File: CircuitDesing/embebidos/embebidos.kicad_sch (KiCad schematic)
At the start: 0 parts

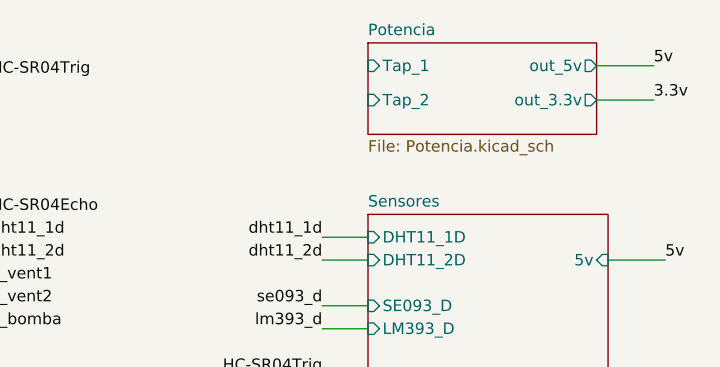
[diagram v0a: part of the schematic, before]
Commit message: pull up
Circuito LDR
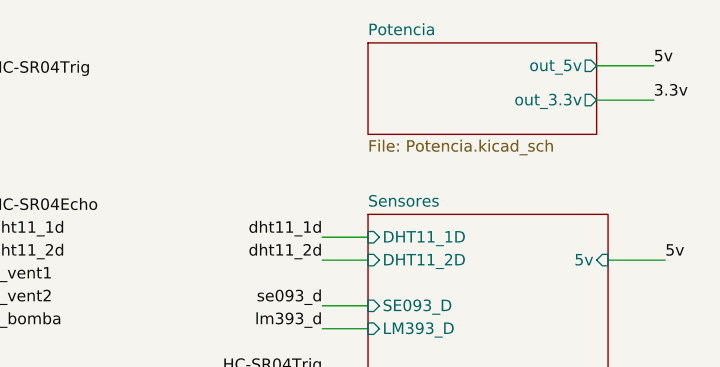
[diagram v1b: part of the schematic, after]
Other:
- sheet Potencia ports: added none; removed Tap_1, Tap_2
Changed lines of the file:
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@@
       (effects (font (size 1.27 1.27)) (justify left top))
-    )
-    (pin "Tap_1" input (at 167.64 62.23 180)
-      (effects (font (size 1.27 1.27)) (justify left))
-    )
-    (pin "Tap_2" input (at 167.64 66.04 180)
-      (effects (font (size 1.27 1.27)) (justify left))
     )
     (pin "out_5v" output (at 193.04 62.23 0)
@@
     (path "/baefe8d2-116f-4132-b22d-e866645ad738" (page "4"))
     (path "/2a66dc13-5d83-46f7-9074-3655609524a8" (page "5"))
-    (path "/2a66dc13-5d83-46f7-9074-3655609524a8/a135e9bb-3dd4-4bac-8875-0b8619cdbde0" (page "7"))
     (path "/2a66dc13-5d83-46f7-9074-3655609524a8/74549759-895a-4805-b4eb-8b7b7d22db26" (page "7"))
     (path "/4a4a8db1-1786-4804-b37e-204adf7255cc/49f3433d-4d41-4994-b007-3fd9fa4c7900" (page "8"))
@@
       (reference "#PWR015") (unit 1) (value "GND") (footprint "")
     )
-    (path "/2a66dc13-5d83-46f7-9074-3655609524a8/88b4c1f2-fa29-42b0-8b8e-d7a406d13c1c"
-      (reference "#PWR016") (unit 1) (value "GND") (footprint "")
-    )
-    (path "/2a66dc13-5d83-46f7-9074-3655609524a8/a135e9bb-3dd4-4bac-8875-0b8619cdbde0/f95e0a6a-1f02-4b13-a777-d73ecda7f4e6"
-      (reference "#PWR017") (unit 1) (value "GND") (footprint "")
-    )
-    (path "/2a66dc13-5d83-46f7-9074-3655609524a8/a135e9bb-3dd4-4bac-8875-0b8619cdbde0/093773d2-48d3-4183-9a42-2d4675e4bd31"
-      (reference "#PWR018") (unit 1) (value "GND") (footprint "")
-    )
-    (path "/2a66dc13-5d83-46f7-9074-3655609524a8/a135e9bb-3dd4-4bac-8875-0b8619cdbde0/cdabb997-2f53-4fa4-a27a-fd81b4d9f5ba"
-      (reference "#PWR019") (unit 1) (value "GND") (footprint "")
-    )
-    (path "/2a66dc13-5d83-46f7-9074-3655609524a8/a135e9bb-3dd4-4bac-8875-0b8619cdbde0/3d119db0-fa20-4eb6-83c6-89997012cb89"
-      (reference "#PWR020") (unit 1) (value "GND") (footprint "")
-    )
     (path "/2a66dc13-5d83-46f7-9074-3655609524a8/74549759-895a-4805-b4eb-8b7b7d22db26/e0179e21-6428-45da-b033-c9fefee37896"
       (reference "#PWR021") (unit 1) (value "GND") (footprint "")
@@
       (reference "#PWR0105") (unit 1) (value "GND") (footprint "")
     )
+    (path "/4a4a8db1-1786-4804-b37e-204adf7255cc/49f3433d-4d41-4994-b007-3fd9fa4c7900/07f61c9e-cf2f-4ff8-971f-bebff896dc30"
+      (reference "#PWR?") (unit 1) (value "GND") (footprint "")
+    )
+    (path "/2a66dc13-5d83-46f7-9074-3655609524a8/14cf2f17-a01d-473c-884e-3c66510750af"
+      (reference "#PWR?") (unit 1) (value "GND") (footprint "")
+    )
     (path "/4a4a8db1-1786-4804-b37e-204adf7255cc/49f3433d-4d41-4994-b007-3fd9fa4c7900/ba8244e2-67ae-47d6-acea-927aaf267f1a"
       (reference "7k1") (unit 1) (value "R") (footprint "Resistor_SMD:R_0603_1608Metric_Pad0.98x0.95mm_HandSolder")
@@
       (reference "10k2") (unit 1) (value "R") (footprint "Resistor_SMD:R_0603_1608Metric_Pad0.98x0.95mm_HandSolder")
     )
+    (path "/4a4a8db1-1786-4804-b37e-204adf7255cc/49f3433d-4d41-4994-b007-3fd9fa4c7900/a970a7de-87f7-4442-a266-d08deb9a3533"
+      (reference "10k?") (unit 1) (value "R") (footprint "Resistor_SMD:R_0603_1608Metric_Pad0.98x0.95mm_HandSolder")
+    )
+    (path "/4a4a8db1-1786-4804-b37e-204adf7255cc/49f3433d-4d41-4994-b007-3fd9fa4c7900/f70f0e83-2200-4c3e-b886-a0a949538d41"
+      (reference "10k?") (unit 1) (value "R") (footprint "Resistor_SMD:R_0603_1608Metric_Pad0.98x0.95mm_HandSolder")
+    )
     (path "/baefe8d2-116f-4132-b22d-e866645ad738/531b805e-c06f-4d99-9a71-e4710c702534"
       (reference "Bomba1") (unit 1) (value "Conn_01x02") (footprint "Connector_JST:JST_EH_B2B-EH-A_1x02_P2.50mm_Vertical")
@@
       (reference "C3") (unit 1) (value "1uF") (footprint "Capacitor_SMD:C_0603_1608Metric_Pad1.08x0.95mm_HandSolder")
     )
-    (path "/2a66dc13-5d83-46f7-9074-3655609524a8/22992aa0-492a-4f8a-8efd-ef43411e8d89"
-      (reference "C4") (unit 1) (value "470u") (footprint "Capacitor_SMD:C_0603_1608Metric_Pad1.08x0.95mm_HandSolder")
-    )
-    (path "/2a66dc13-5d83-46f7-9074-3655609524a8/a135e9bb-3dd4-4bac-8875-0b8619cdbde0/835aa7da-68b4-44c2-9904-d9907768c770"
-      (reference "C5") (unit 1) (value "100u") (footprint "Capacitor_SMD:C_0603_1608Metric_Pad1.08x0.95mm_HandSolder")
-    )
-    (path "/2a66dc13-5d83-46f7-9074-3655609524a8/a135e9bb-3dd4-4bac-8875-0b8619cdbde0/aa171677-d82f-431a-b3b8-9da407e60c75"
-      (reference "C6") (unit 1) (value "1000u") (footprint "Capacitor_SMD:C_0603_1608Metric_Pad1.08x0.95mm_HandSolder")
-    )
     (path "/2a66dc13-5d83-46f7-9074-3655609524a8/74549759-895a-4805-b4eb-8b7b7d22db26/e7cbd5f0-969e-4721-864f-6bd2229333d2"
       (reference "C7") (unit 1) (value "10u") (footprint "Capacitor_SMD:C_0603_1608Metric_Pad1.08x0.95mm_HandSolder")
@@
       (reference "C8") (unit 1) (value "100u") (footprint "Capacitor_SMD:C_0603_1608Metric_Pad1.08x0.95mm_HandSolder")
     )
-    (path "/2a66dc13-5d83-46f7-9074-3655609524a8/6c70350e-eac4-4182-b931-ca24aa40b677"
-      (reference "D1") (unit 1) (value "1N5822") (footprint "Diode_THT:D_DO-201AD_P15.24mm_Horizontal")
-    )
-    (path "/2a66dc13-5d83-46f7-9074-3655609524a8/a89a4a92-173e-447f-b20b-23fe2eb34209"
-      (reference "D2") (unit 1) (value "1N5822") (footprint "Diode_THT:D_DO-201AD_P15.24mm_Horizontal")
-    )
-    (path "/2a66dc13-5d83-46f7-9074-3655609524a8/912ccca9-f753-45a8-8c37-ed2d1fe140a9"
-      (reference "D3") (unit 1) (value "1N5822") (footprint "Diode_THT:D_DO-201AD_P15.24mm_Horizontal")
-    )
-    (path "/2a66dc13-5d83-46f7-9074-3655609524a8/35cafbd7-5e9c-4d45-bbef-44f7ba0cc91d"
-      (reference "D4") (unit 1) (value "1N5822") (footprint "Diode_THT:D_DO-201AD_P15.24mm_Horizontal")
-    )
-    (path "/2a66dc13-5d83-46f7-9074-3655609524a8/a135e9bb-3dd4-4bac-8875-0b8619cdbde0/53a1f403-a76e-4aed-b037-28faac0deb6d"
-      (reference "D5") (unit 1) (value "1N5822") (footprint "Diode_THT:D_DO-201AD_P15.24mm_Horizontal")
-    )
     (path "/baefe8d2-116f-4132-b22d-e866645ad738/39e61f26-6263-4692-8217-981d38a508b6"
       (reference "D6") (unit 1) (value "LED") (footprint "LED_SMD:LED_0603_1608Metric_Pad1.05x0.95mm_HandSolder")
@@
       (reference "J1") (unit 1) (value "Conn_01x02") (footprint "Connector_JST:JST_EH_B2B-EH-A_1x02_P2.50mm_Vertical")
     )
-    (path "/2a66dc13-5d83-46f7-9074-3655609524a8/a135e9bb-3dd4-4bac-8875-0b8619cdbde0/810ad703-c27e-4129-9cf8-0a0a3d8c9560"
-      (reference "L1") (unit 1) (value "100u") (footprint "Inductor_SMD:L_0603_1608Metric_Pad1.05x0.95mm_HandSolder")
+    (path "/2a66dc13-5d83-46f7-9074-3655609524a8/6d7054e4-fed7-4014-bfc1-bf169b5ca941"
+      (reference "J?") (unit 1) (value "USB_B_Micro") (footprint "")
     )
     (path "/baefe8d2-116f-4132-b22d-e866645ad738/300b40b9-0f22-49e2-89f3-427fcd3d7cfd"
@@
       (reference "Q3") (unit 1) (value "IRF540N") (footprint "Package_TO_SOT_THT:TO-220-3_Vertical")
     )
+    (path "/4a4a8db1-1786-4804-b37e-204adf7255cc/49f3433d-4d41-4994-b007-3fd9fa4c7900/d4e796dc-ad9d-497f-8f2d-f53f94bdbd8e"
+      (reference "Q?") (unit 1) (value "2N2219") (footprint "Package_TO_SOT_THT:TO-39-3")
+    )
     (path "/255ea3b8-af73-4dd8-9773-761204920633/d01d708b-9141-4761-81a4-1d1bb9480e12"
       (reference "R1") (unit 1) (value "10k") (footprint "Resistor_SMD:R_0603_1608Metric_Pad0.98x0.95mm_HandSolder")
@@
       (reference "R7") (unit 1) (value "1k") (footprint "Resistor_SMD:R_0603_1608Metric_Pad0.98x0.95mm_HandSolder")
     )
+    (path "/4a4a8db1-1786-4804-b37e-204adf7255cc/49f3433d-4d41-4994-b007-3fd9fa4c7900/aaa0c7cc-fb60-4232-9eee-0520be77ad34"
+      (reference "R?") (unit 1) (value "R") (footprint "")
+    )
     (path "/4a4a8db1-1786-4804-b37e-204adf7255cc/52ecff1d-2404-40d4-b3d5-28684b4d8d27"
       (reference "SE93") (unit 1) (value "Conn_01x03") (footprint "Connector_JST:JST_EH_B3B-EH-A_1x03_P2.50mm_Vertical")
@@
       (reference "U1") (unit 1) (value "ESP32-WROOM-32") (footprint "RF_Module:ESP32-WROOM-32")
     )
-    (path "/2a66dc13-5d83-46f7-9074-3655609524a8/a135e9bb-3dd4-4bac-8875-0b8619cdbde0/9bfa7db7-3d9d-48b0-b783-973fddb7ad49"
-      (reference "U2") (unit 1) (value "LM2576S-5") (footprint "Package_TO_SOT_SMD:TO-263-5_TabPin3")
-    )
     (path "/2a66dc13-5d83-46f7-9074-3655609524a8/74549759-895a-4805-b4eb-8b7b7d22db26/daf9f53c-8abd-49fa-af52-0797e9e7ee97"

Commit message: Actualizacion huellas
Huellas+Programador
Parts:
- added J_I2C1: Conn_01x05_Male, Connector_PinSocket_2.54mm:PinSocket_1x05_P2.54mm_Horizontal, symbol Connector:Conn_01x05_Male
- added J_prog1: Conn_01x06_Male, Connector_PinHeader_2.54mm:PinHeader_1x06_P2.54mm_Horizontal, symbol Connector:Conn_01x06_Male
- added L_p1: LED, LED_SMD:LED_0805_2012Metric_Pad1.15x1.40mm_HandSolder, symbol Device:LED
- added RCL1, RDA1: 10k, Resistor_SMD:R_0805_2012Metric_Pad1.20x1.40mm_HandSolder, symbol Device:R
- added R_p1: 47, Resistor_SMD:R_0805_2012Metric_Pad1.20x1.40mm_HandSolder, symbol Device:R
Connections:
- net 3.3v: now also J_I2C1.4 (Pin_4), RCL1.2, RDA1.2
- net 5v: now also J_I2C1.5 (Pin_5)
- new net: L_p1.2 (A), R_p1.1
- new net GND: J_I2C1.3 (Pin_3), J_prog1.5 (Pin_5), L_p1.1 (K)
- new net LedU1: R_p1.2
- new net Prog_Rx: J_prog1.3 (Pin_3)
- new net Prog_Tx: J_prog1.4 (Pin_4)
- new net SCL: J_I2C1.1 (Pin_1), RCL1.1
- new net SDA: J_I2C1.2 (Pin_2), RDA1.1
- no-connect marks 0 -> 3
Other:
- sheet Esp32Schematic ports: added LedU; removed none
- note added: "LED_Programmer"
- note added: "Pines libres"
- note added: "USB_Programmer"

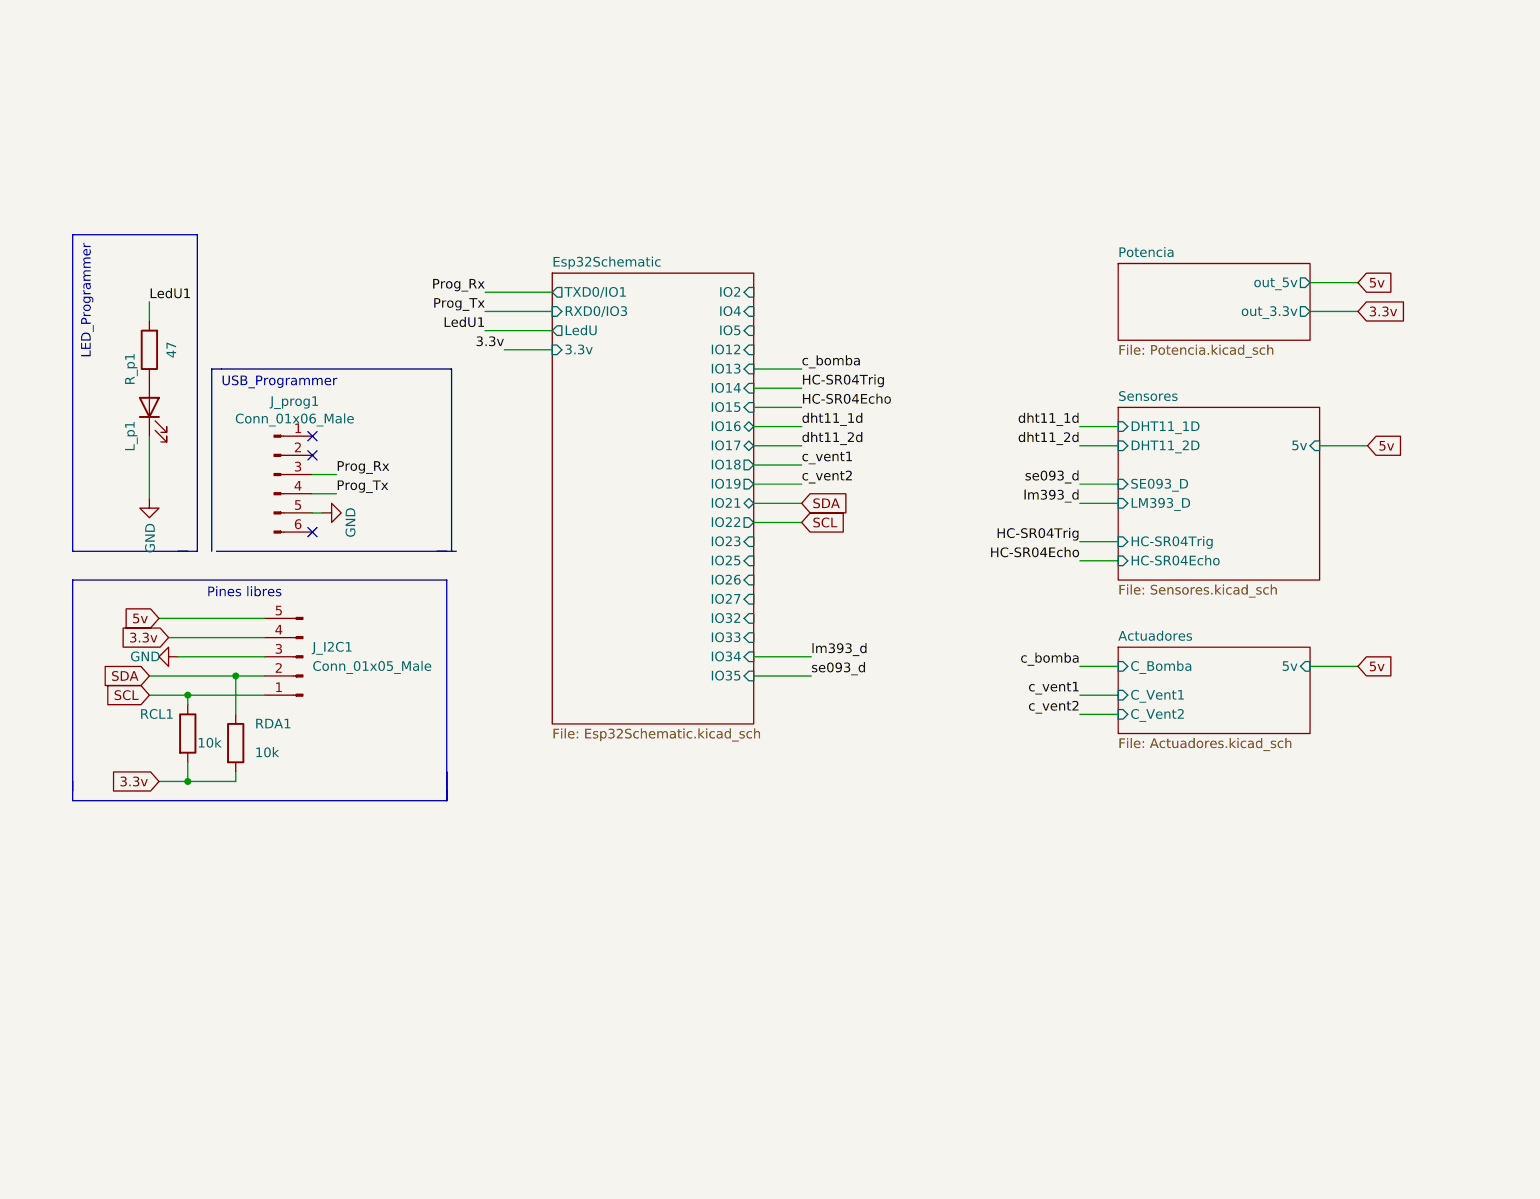
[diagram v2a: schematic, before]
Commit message: Coversores lógicos + alertas + humidificador
Coversores lógicos + alertas + humidificador
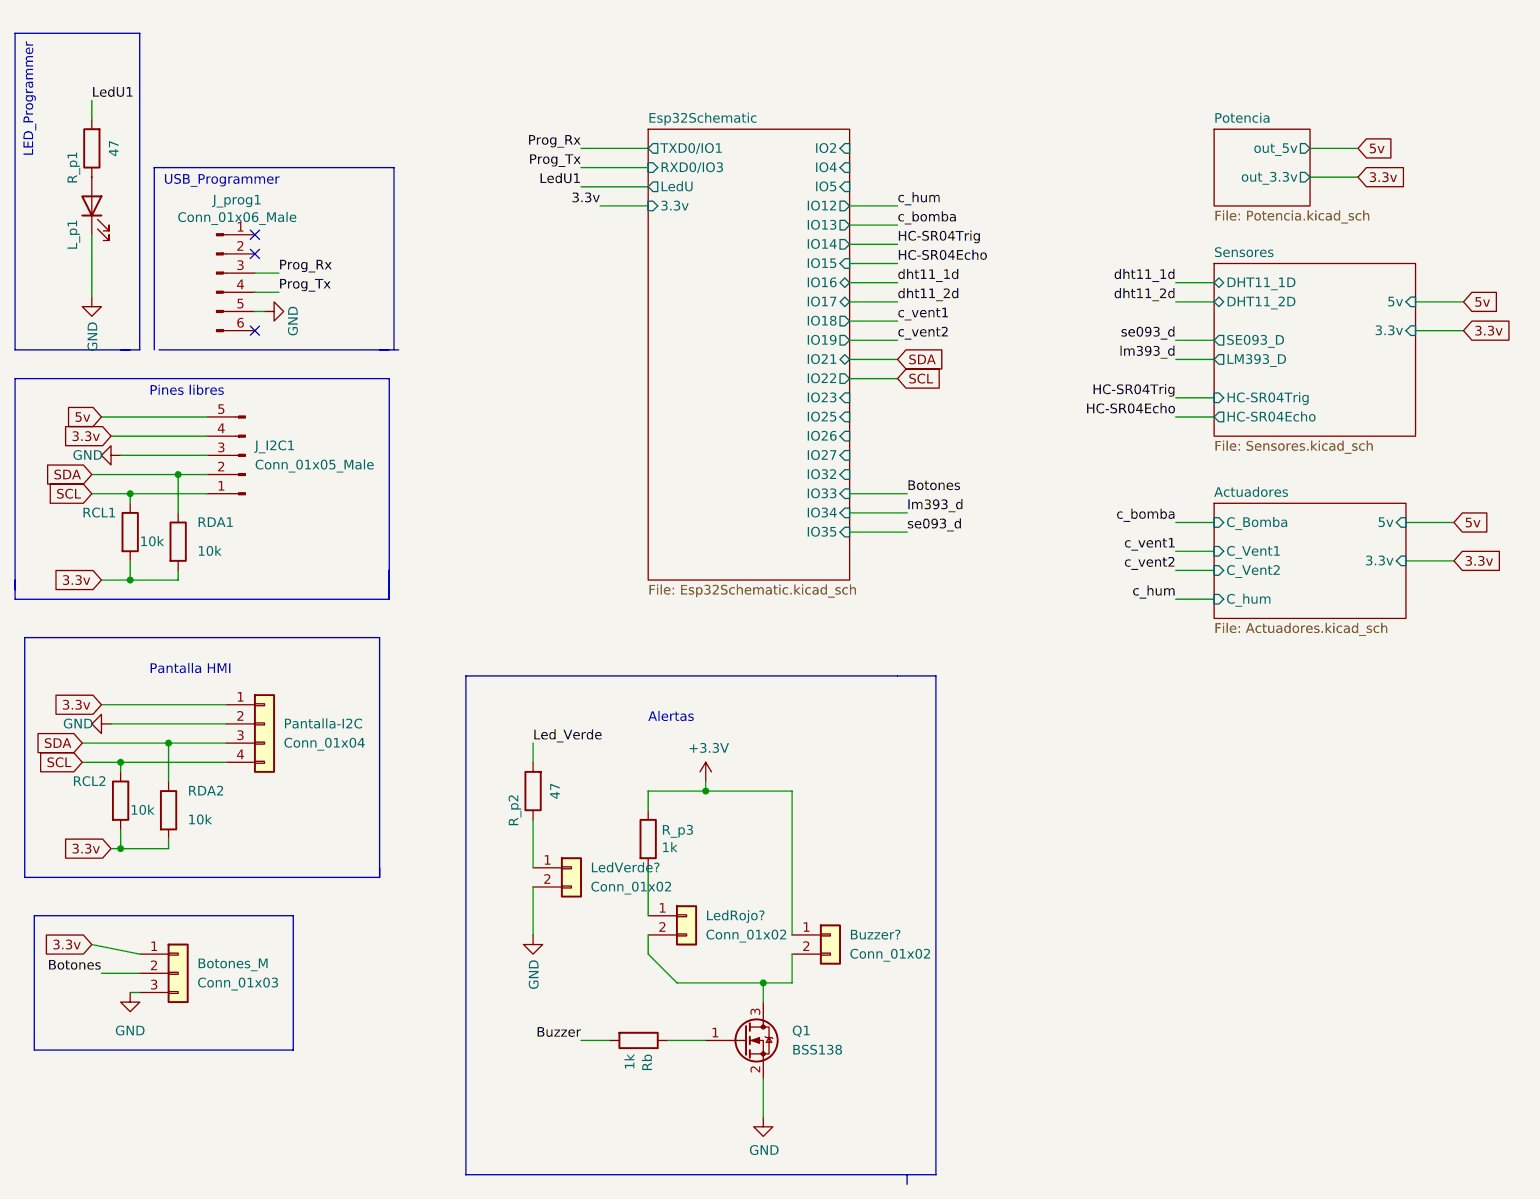
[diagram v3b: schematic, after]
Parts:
- added Botones_M: Conn_01x03, Connector_JST:JST_EH_B3B-EH-A_1x03_P2.50mm_Vertical, symbol Connector_Generic:Conn_01x03
- added Buzzer?, LedRojo?, LedVerde?: Conn_01x02, symbol Connector_Generic:Conn_01x02
- added Pantalla-I2C: Conn_01x04, Connector_JST:JST_EH_B4B-EH-A_1x04_P2.50mm_Vertical, symbol Connector_Generic:Conn_01x04
- added Q1: BSS138, Package_TO_SOT_SMD:SOT-23, symbol Transistor_FET:BSS138
- added RCL2, RDA2: 10k, Resistor_SMD:R_0805_2012Metric_Pad1.20x1.40mm_HandSolder, symbol Device:R
- added R_p2: 47, Resistor_SMD:R_0805_2012Metric_Pad1.20x1.40mm_HandSolder, symbol Device:R
- added R_p3: 1k, symbol Device:R
- added Rb: 1k, Resistor_SMD:R_0603_1608Metric_Pad0.98x0.95mm_HandSolder, symbol Device:R
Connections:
- net 3.3v: now also Botones_M.1 (Pin_1), Pantalla-I2C.1 (Pin_1), RCL2.2, RDA2.2
- net GND: now also Botones_M.3 (Pin_3), LedVerde?.2 (Pin_2), Pantalla-I2C.2 (Pin_2), Q1.2 (S)
- net SCL: now also Pantalla-I2C.4 (Pin_4), RCL2.1
- net SDA: now also Pantalla-I2C.3 (Pin_3), RDA2.1
- new net: LedVerde?.1 (Pin_1), R_p2.1
- new net: LedRojo?.1 (Pin_1), R_p3.2
- new net: Q1.1 (G), Rb.1
- new net: Buzzer?.2 (Pin_2), LedRojo?.2 (Pin_2), Q1.3 (D)
- new net +3V3: Buzzer?.1 (Pin_1), R_p3.1
- new net Botones: Botones_M.2 (Pin_2)
- new net Buzzer: Rb.2
- new net Led_Verde: R_p2.2
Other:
- sheet Actuadores ports: added 3.3v, C_hum; removed none
- sheet Sensores ports: added 3.3v; removed none
- note added: "Alertas"
- note added: "Pantalla HMI"
- moved on the sheet: J_I2C1, J_prog1, L_p1, RCL1, RDA1, R_p1
